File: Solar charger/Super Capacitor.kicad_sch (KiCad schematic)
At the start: 16 parts, among them U2 BW6101_, U3 BW6101_, U4 BW6101_, U5 BW6101_

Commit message: board compelet
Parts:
- R10: renamed from R5; footprint (none) -> Resistor_SMD:R_0805_2012Metric
- R11: renamed from R6; footprint (none) -> Resistor_SMD:R_0805_2012Metric
- R12: renamed from R7; footprint (none) -> Resistor_SMD:R_0805_2012Metric
- R9: renamed from R4; footprint (none) -> Resistor_SMD:R_0805_2012Metric
- renumbered C2 to C10, C3 to C11, C4 to C12, C5 to C13, C6 to C14, C7 to C15, C8 to C16, C1 to C9
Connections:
- net at R12.1: now also U5.5 (IOUT); no longer U5.6 (IOUT)
- net at R10.1: now also U3.5 (IOUT); no longer U3.6 (IOUT)
- net at U2.5 (IOUT): now also R9.1
- net at R11.1: now also U4.5 (IOUT); no longer U4.6 (IOUT)
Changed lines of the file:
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@@
   (symbol (lib_id "Device:C_Polarized_US") (at 118.11 110.49 0) (unit 1)
     (in_bom yes) (on_board yes) (fields_autoplaced)
-    (property "Reference" "C3" (id 0) (at 121.92 108.5849 0)
+    (property "Reference" "C11" (id 0) (at 121.92 108.5849 0)
       (effects (font (size 1.27 1.27)) (justify left))
     )
@@
   (symbol (lib_id "Device:R_US") (at 165.1 134.62 0) (unit 1)
     (in_bom yes) (on_board yes) (fields_autoplaced)
-    (property "Reference" "R7" (id 0) (at 167.64 133.3499 0)
+    (property "Reference" "R12" (id 0) (at 167.64 133.3499 0)
       (effects (font (size 1.27 1.27)) (justify left))
     )
@@
       (effects (font (size 1.27 1.27)) (justify left))
     )
-    (property "Footprint" "" (id 2) (at 166.116 134.874 90)
+    (property "Footprint" "Resistor_SMD:R_0805_2012Metric" (id 2) (at 166.116 134.874 90)
       (effects (font (size 1.27 1.27)) hide)
     )
@@
   (symbol (lib_id "Device:R_US") (at 165.1 86.36 0) (unit 1)
     (in_bom yes) (on_board yes) (fields_autoplaced)
-    (property "Reference" "R5" (id 0) (at 167.64 85.0899 0)
+    (property "Reference" "R10" (id 0) (at 167.64 85.0899 0)
       (effects (font (size 1.27 1.27)) (justify left))
     )
@@
       (effects (font (size 1.27 1.27)) (justify left))
     )
-    (property "Footprint" "" (id 2) (at 166.116 86.614 90)
+    (property "Footprint" "Resistor_SMD:R_0805_2012Metric" (id 2) (at 166.116 86.614 90)
       (effects (font (size 1.27 1.27)) hide)
     )
@@
     (pin "2")
   )
-  (symbol (lib_name "BW6101__1") (lib_id "1_Resouce:BW6101_") (at 151.13 59.69 0) (unit 1)
+  (symbol (lib_id "1_Resouce:BW6101_") (at 151.13 59.69 0) (unit 1)
     (in_bom yes) (on_board yes) (fields_autoplaced)
     (property "Reference" "U2" (id 0) (at 151.13 48.26 0))
@@
     (pin "2")
     (pin "3")
-    (pin "5")
-    (pin "6")
+    (pin "4")
+    (pin "5")
   )
   (symbol (lib_id "Device:C_Polarized_US") (at 118.11 134.62 0) (unit 1)
     (in_bom yes) (on_board yes) (fields_autoplaced)
-    (property "Reference" "C4" (id 0) (at 121.92 132.7149 0)
+    (property "Reference" "C12" (id 0) (at 121.92 132.7149 0)
       (effects (font (size 1.27 1.27)) (justify left))
     )
@@
     (pin "2")
     (pin "3")
-    (pin "5")
-    (pin "6")
+    (pin "4")
+    (pin "5")
   )
   (symbol (lib_id "Device:C") (at 130.81 110.49 0) (unit 1)
     (in_bom yes) (on_board yes) (fields_autoplaced)
-    (property "Reference" "C7" (id 0) (at 134.62 109.2199 0)
+    (property "Reference" "C15" (id 0) (at 134.62 109.2199 0)
       (effects (font (size 1.27 1.27)) (justify left))
     )
@@
   (symbol (lib_id "Device:C") (at 130.81 62.23 0) (unit 1)
     (in_bom yes) (on_board yes) (fields_autoplaced)
-    (property "Reference" "C5" (id 0) (at 134.62 60.9599 0)
+    (property "Reference" "C13" (id 0) (at 134.62 60.9599 0)
       (effects (font (size 1.27 1.27)) (justify left))
     )
@@
     (pin "2")
   )
-  (symbol (lib_name "BW6101__3") (lib_id "1_Resouce:BW6101_") (at 151.13 132.08 0) (unit 1)
+  (symbol (lib_id "1_Resouce:BW6101_") (at 151.13 132.08 0) (unit 1)
     (in_bom yes) (on_board yes) (fields_autoplaced)
     (property "Reference" "U5" (id 0) (at 151.13 120.65 0))
@@
     (pin "2")
     (pin "3")
-    (pin "5")
-    (pin "6")
+    (pin "4")
+    (pin "5")
   )
   (symbol (lib_id "Device:C_Polarized_US") (at 118.11 86.36 0) (unit 1)
     (in_bom yes) (on_board yes) (fields_autoplaced)
-    (property "Reference" "C2" (id 0) (at 121.92 84.4549 0)
+    (property "Reference" "C10" (id 0) (at 121.92 84.4549 0)
       (effects (font (size 1.27 1.27)) (justify left))
     )
@@
   (symbol (lib_id "Device:R_US") (at 165.1 62.23 0) (unit 1)
     (in_bom yes) (on_board yes) (fields_autoplaced)
-    (property "Reference" "R4" (id 0) (at 167.64 60.9599 0)
+    (property "Reference" "R9" (id 0) (at 167.64 60.9599 0)
       (effects (font (size 1.27 1.27)) (justify left))
     )
@@
       (effects (font (size 1.27 1.27)) (justify left))
     )
-    (property "Footprint" "" (id 2) (at 166.116 62.484 90)
+    (property "Footprint" "Resistor_SMD:R_0805_2012Metric" (id 2) (at 166.116 62.484 90)
       (effects (font (size 1.27 1.27)) hide)
     )
@@
   (symbol (lib_id "Device:R_US") (at 165.1 110.49 0) (unit 1)
     (in_bom yes) (on_board yes) (fields_autoplaced)
-    (property "Reference" "R6" (id 0) (at 167.64 109.2199 0)
+    (property "Reference" "R11" (id 0) (at 167.64 109.2199 0)
       (effects (font (size 1.27 1.27)) (justify left))
     )
@@
       (effects (font (size 1.27 1.27)) (justify left))
     )
-    (property "Footprint" "" (id 2) (at 166.116 110.744 90)
+    (property "Footprint" "Resistor_SMD:R_0805_2012Metric" (id 2) (at 166.116 110.744 90)
       (effects (font (size 1.27 1.27)) hide)
     )
@@
   (symbol (lib_id "Device:C") (at 130.81 134.62 0) (unit 1)
     (in_bom yes) (on_board yes) (fields_autoplaced)
-    (property "Reference" "C8" (id 0) (at 134.62 133.3499 0)
+    (property "Reference" "C16" (id 0) (at 134.62 133.3499 0)
       (effects (font (size 1.27 1.27)) (justify left))
     )
@@
     (pin "2")
   )
-  (symbol (lib_name "BW6101__2") (lib_id "1_Resouce:BW6101_") (at 151.13 107.95 0) (unit 1)
+  (symbol (lib_name "BW6101__1") (lib_id "1_Resouce:BW6101_") (at 151.13 107.95 0) (unit 1)
     (in_bom yes) (on_board yes) (fields_autoplaced)
     (property "Reference" "U4" (id 0) (at 151.13 96.52 0))
@@
     (pin "2")
     (pin "3")
-    (pin "5")
-    (pin "6")
+    (pin "4")
+    (pin "5")
   )
   (symbol (lib_id "Device:C_Polarized_US") (at 118.11 62.23 0) (unit 1)
     (in_bom yes) (on_board yes) (fields_autoplaced)
-    (property "Reference" "C1" (id 0) (at 121.92 60.3249 0)
+    (property "Reference" "C9" (id 0) (at 121.92 60.3249 0)
       (effects (font (size 1.27 1.27)) (justify left))
     )
@@
   (symbol (lib_id "Device:C") (at 130.81 86.36 0) (unit 1)
     (in_bom yes) (on_board yes) (fields_autoplaced)
-    (property "Reference" "C6" (id 0) (at 134.62 85.0899 0)
-      (effects (font (size 1.27 1.27)) (justify left))
-    )
+    (property "Reference" "C14" (id 0) (at 134.62 85.0899 0)
+      (effects (font (size 1.27 1.27)) (justify left))
+    )

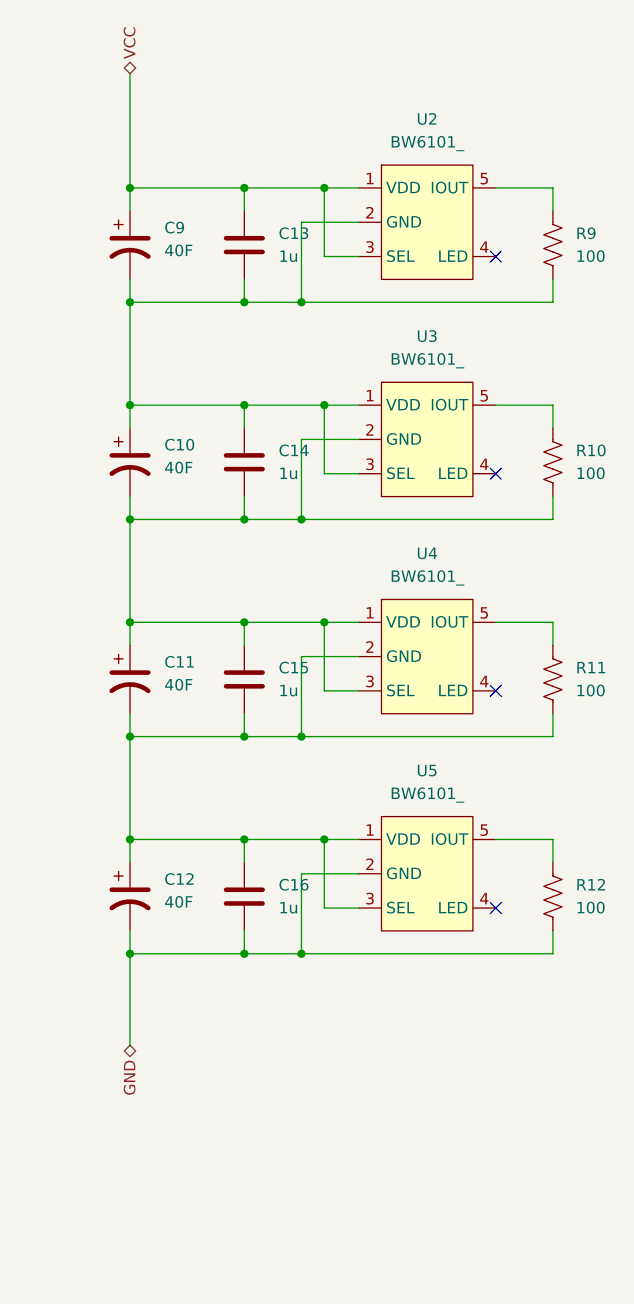
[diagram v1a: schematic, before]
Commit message: 增加電路圖PDF，新增修改一些元件
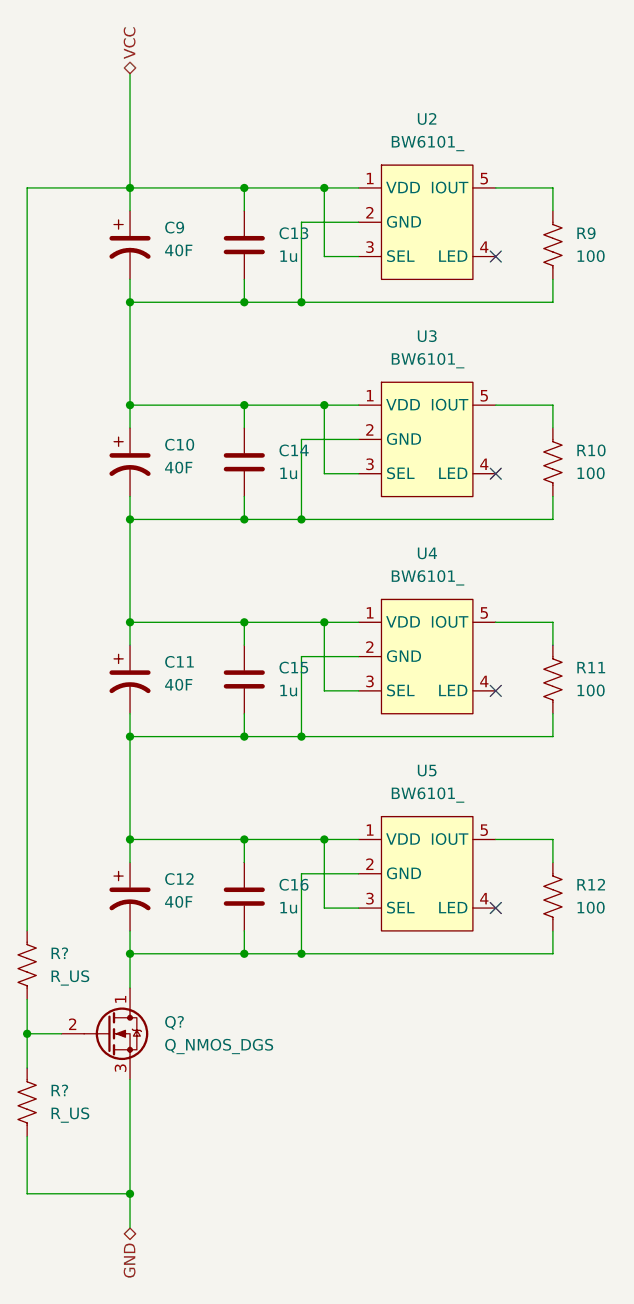
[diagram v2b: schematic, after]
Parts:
- added Q?: Q_NMOS_DGS, symbol Device:Q_NMOS_DGS
- added R? (x2): R_US, symbol Device:R_US
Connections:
- net GND: now also Q?.3 (S), R?.2; no longer C12.2, C16.2, R12.2, U5.2 (GND)
- net VCC: now also R?.1
- new net: C12.2, C16.2, Q?.1 (D), R12.2, U5.2 (GND)
- new net: Q?.2 (G), R?.1, R?.2
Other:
- title: (none) -> Super capacitors 4S with soft start
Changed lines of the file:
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@@
 (kicad_sch (version 20211123) (generator eeschema)
   (paper "A4")
+  (title_block
+    (title "Super capacitors 4S with soft start")
+  )
   (junction (at 118.11 55.88) (diameter 0) (color 0 0 0 0)
   )
@@
   (junction (at 130.81 128.27) (diameter 0) (color 0 0 0 0)
   )
+  (junction (at 106.68 149.86) (diameter 0) (color 0 0 0 0)
+  )
   (junction (at 130.81 104.14) (diameter 0) (color 0 0 0 0)
   )
@@
   )
   (junction (at 139.7 104.14) (diameter 0) (color 0 0 0 0)
+  )
+  (junction (at 118.11 167.64) (diameter 0) (color 0 0 0 0)
   )
   (junction (at 118.11 80.01) (diameter 0) (color 0 0 0 0)
@@
   (no_connect (at 158.75 87.63))
   (no_connect (at 158.75 135.89))
+  (wire (pts (xy 106.68 55.88) (xy 118.11 55.88))
+    (stroke (width 0) (type default) (color 0 0 0 0))
+  )
   (wire (pts (xy 165.1 66.04) (xy 165.1 68.58))
     (stroke (width 0) (type default) (color 0 0 0 0))
@@
     (stroke (width 0) (type default) (color 0 0 0 0))
   )
+  (wire (pts (xy 106.68 146.05) (xy 106.68 149.86))
+    (stroke (width 0) (type default) (color 0 0 0 0))
+  )
   (wire (pts (xy 130.81 90.17) (xy 130.81 92.71))
     (stroke (width 0) (type default) (color 0 0 0 0))
   )
+  (wire (pts (xy 118.11 154.94) (xy 118.11 167.64))
+    (stroke (width 0) (type default) (color 0 0 0 0))
+  )
   (wire (pts (xy 137.16 140.97) (xy 130.81 140.97))
     (stroke (width 0) (type default) (color 0 0 0 0))
   )
+  (wire (pts (xy 106.68 149.86) (xy 106.68 153.67))
+    (stroke (width 0) (type default) (color 0 0 0 0))
+  )
+  (wire (pts (xy 106.68 161.29) (xy 106.68 167.64))
+    (stroke (width 0) (type default) (color 0 0 0 0))
+  )
   (wire (pts (xy 158.75 104.14) (xy 165.1 104.14))
     (stroke (width 0) (type default) (color 0 0 0 0))
@@
     (stroke (width 0) (type default) (color 0 0 0 0))
   )
+  (wire (pts (xy 118.11 167.64) (xy 118.11 171.45))
+    (stroke (width 0) (type default) (color 0 0 0 0))
+  )
+  (wire (pts (xy 106.68 138.43) (xy 106.68 55.88))
+    (stroke (width 0) (type default) (color 0 0 0 0))
+  )
   (wire (pts (xy 165.1 104.14) (xy 165.1 106.68))
     (stroke (width 0) (type default) (color 0 0 0 0))
   )
+  (wire (pts (xy 106.68 149.86) (xy 110.49 149.86))
+    (stroke (width 0) (type default) (color 0 0 0 0))
+  )
+  (wire (pts (xy 106.68 167.64) (xy 118.11 167.64))
+    (stroke (width 0) (type default) (color 0 0 0 0))
+  )
   (wire (pts (xy 118.11 128.27) (xy 130.81 128.27))
     (stroke (width 0) (type default) (color 0 0 0 0))
@@
     (stroke (width 0) (type default) (color 0 0 0 0))
   )
-  (wire (pts (xy 118.11 140.97) (xy 118.11 151.13))
+  (wire (pts (xy 118.11 140.97) (xy 118.11 144.78))
     (stroke (width 0) (type default) (color 0 0 0 0))
   )
@@
     (effects (font (size 1.27 1.27)) (justify left))
   )
-  (hierarchical_label "GND" (shape bidirectional) (at 118.11 151.13 270)
+  (hierarchical_label "GND" (shape bidirectional) (at 118.11 171.45 270)
     (effects (font (size 1.27 1.27)) (justify right))
   )
@@
     )
     (property "Datasheet" "~" (id 3) (at 165.1 86.36 0)
+      (effects (font (size 1.27 1.27)) hide)
+    )
+    (pin "1")
+    (pin "2")
+  )
+  (symbol (lib_id "Device:R_US") (at 106.68 157.48 0) (unit 1)
+    (in_bom yes) (on_board yes) (fields_autoplaced)
+    (property "Reference" "R?" (id 0) (at 109.22 156.2099 0)
+      (effects (font (size 1.27 1.27)) (justify left))
+    )
+    (property "Value" "R_US" (id 1) (at 109.22 158.7499 0)
+      (effects (font (size 1.27 1.27)) (justify left))
+    )
+    (property "Footprint" "" (id 2) (at 107.696 157.734 90)
+      (effects (font (size 1.27 1.27)) hide)
+    )
+    (property "Datasheet" "~" (id 3) (at 106.68 157.48 0)
       (effects (font (size 1.27 1.27)) hide)
     )
@@
     (pin "5")
   )
+  (symbol (lib_id "Device:Q_NMOS_DGS") (at 115.57 149.86 0) (unit 1)
+    (in_bom yes) (on_board yes) (fields_autoplaced)
+    (property "Reference" "Q?" (id 0) (at 121.92 148.5899 0)
+      (effects (font (size 1.27 1.27)) (justify left))
+    )
+    (property "Value" "Q_NMOS_DGS" (id 1) (at 121.92 151.1299 0)
+      (effects (font (size 1.27 1.27)) (justify left))
+    )
+    (property "Footprint" "" (id 2) (at 120.65 147.32 0)
+      (effects (font (size 1.27 1.27)) hide)
+    )
+    (property "Datasheet" "~" (id 3) (at 115.57 149.86 0)
+      (effects (font (size 1.27 1.27)) hide)
+    )
+    (pin "1")
+    (pin "2")
+    (pin "3")
+  )
   (symbol (lib_id "Device:C") (at 130.81 110.49 0) (unit 1)
     (in_bom yes) (on_board yes) (fields_autoplaced)
@@
       (effects (font (size 1.27 1.27)) hide)
     )
+    (pin "1")
+    (pin "2")
+  )
+  (symbol (lib_id "Device:R_US") (at 106.68 142.24 0) (unit 1)
+    (in_bom yes) (on_board yes) (fields_autoplaced)
+    (property "Reference" "R?" (id 0) (at 109.22 140.9699 0)
+      (effects (font (size 1.27 1.27)) (justify left))
+    )
+    (property "Value" "R_US" (id 1) (at 109.22 143.5099 0)
+      (effects (font (size 1.27 1.27)) (justify left))
+    )
+    (property "Footprint" "" (id 2) (at 107.696 142.494 90)
+      (effects (font (size 1.27 1.27)) hide)
+    )
+    (property "Datasheet" "~" (id 3) (at 106.68 142.24 0)
+      (effects (font (size 1.27 1.27)) hide)
+    )
